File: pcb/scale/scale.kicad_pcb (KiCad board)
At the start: 2 copper layers, 103.8 x 47.9 mm, 86 parts, among them J1 USB_C_Receptacle_USB2.0, J2 Conn_01x07, J3 Conn_01x04, SW1 SW_Push, SW10 SW_Push, SW11 SW_Push, SW12 SW_Push, SW13 SW_Push, SW14 SW_Push, SW15 SW_Push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

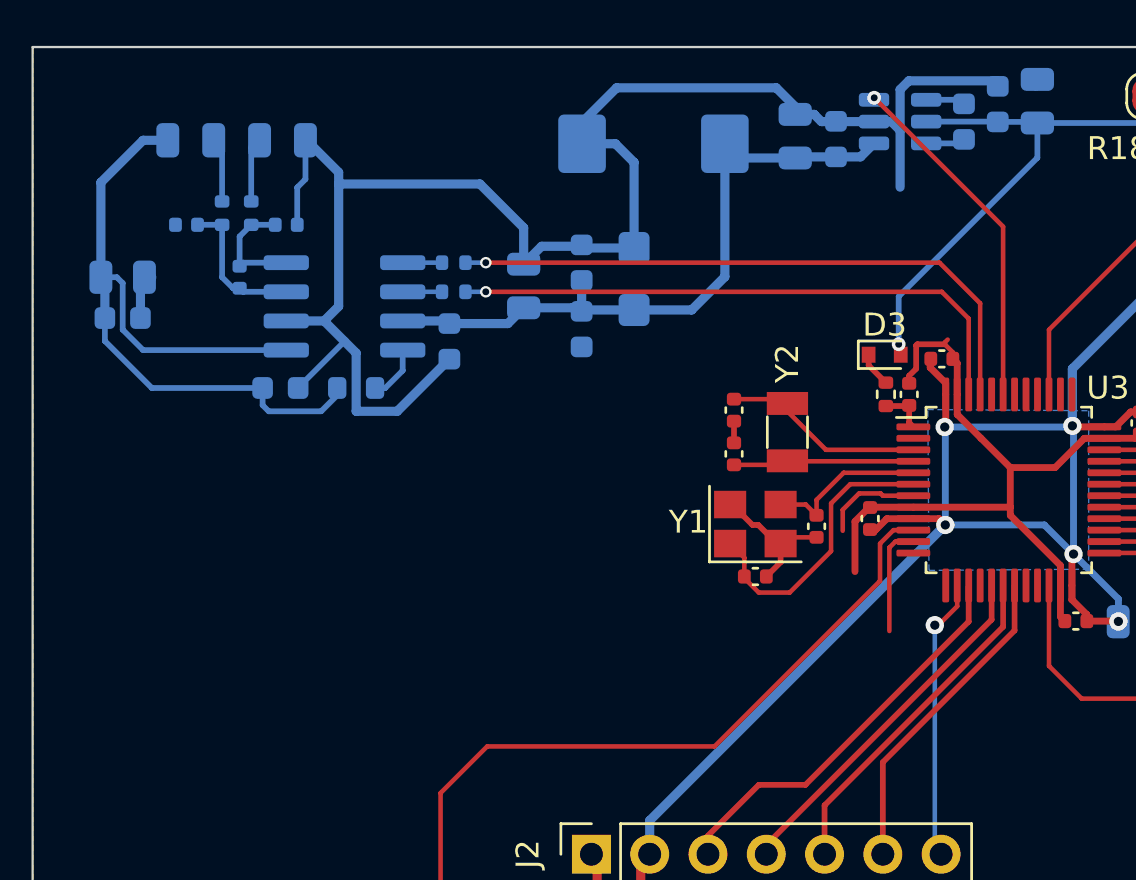
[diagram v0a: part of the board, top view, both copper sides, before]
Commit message: 移除0402元件位号，添加NRST和BOOT0电路
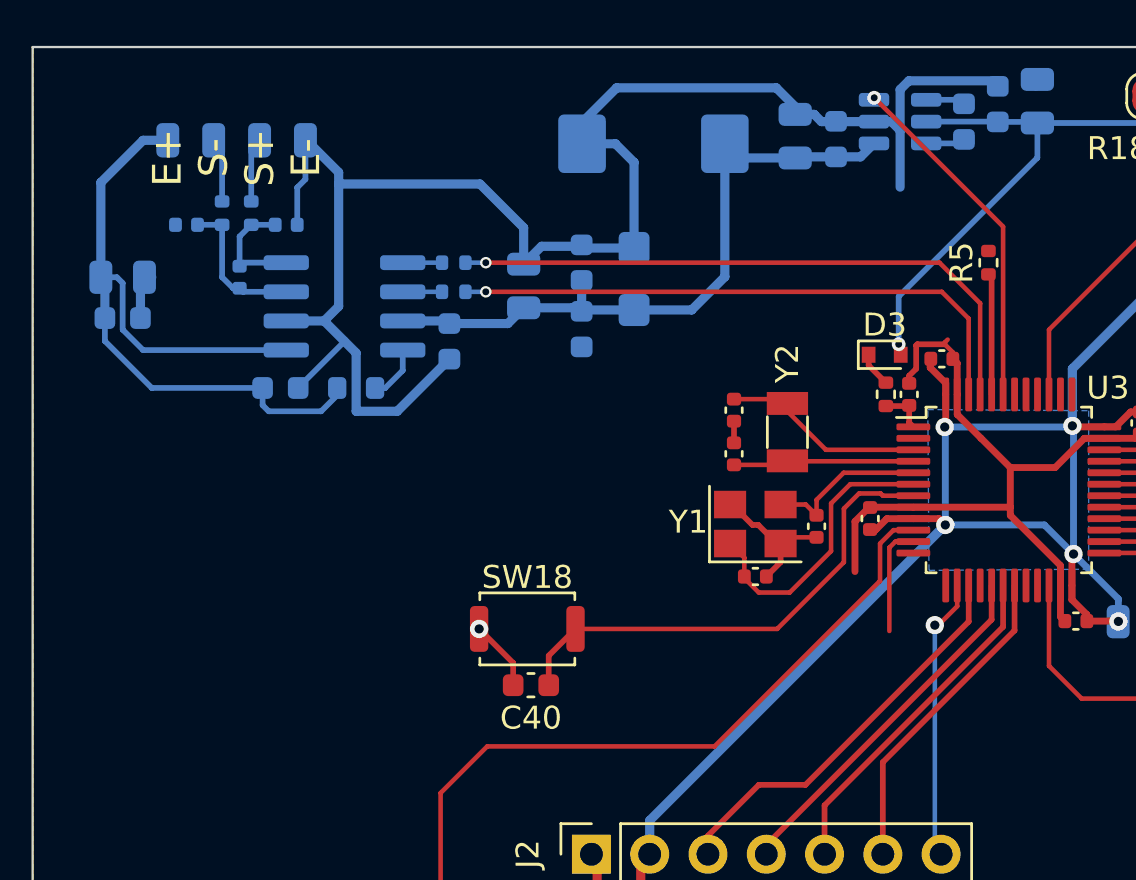
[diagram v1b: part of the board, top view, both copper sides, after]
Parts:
- added C40: 100n, Capacitor_SMD:C_0603_1608Metric, F.Cu at (90.8, 78.6)
- added R5: 47k, Resistor_SMD:R_0402_1005Metric, F.Cu at (110.7, 60.2)
- added SW18: SW_Push, Button_Switch_SMD:SW_Push_SPST_NO_Alps_SKRK, F.Cu at (90.6, 76.2)
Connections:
- U3 pad 44: unconnected-(U3-Pad44) -> /BOOT0
- U3 pad 7: unconnected-(U3-Pad7) -> /NRST
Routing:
- net /NRST: track 0.00 -> 21.5 mm
- net /BOOT0: track 0.00 -> 5.29 mm
- net unconnected-(U3-Pad7): track 4.33 -> 0.00 mm
- net GND: track 187.3 -> 190.4 mm, vias 2 -> 3
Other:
- board text added: "E+ S- S+ E-"

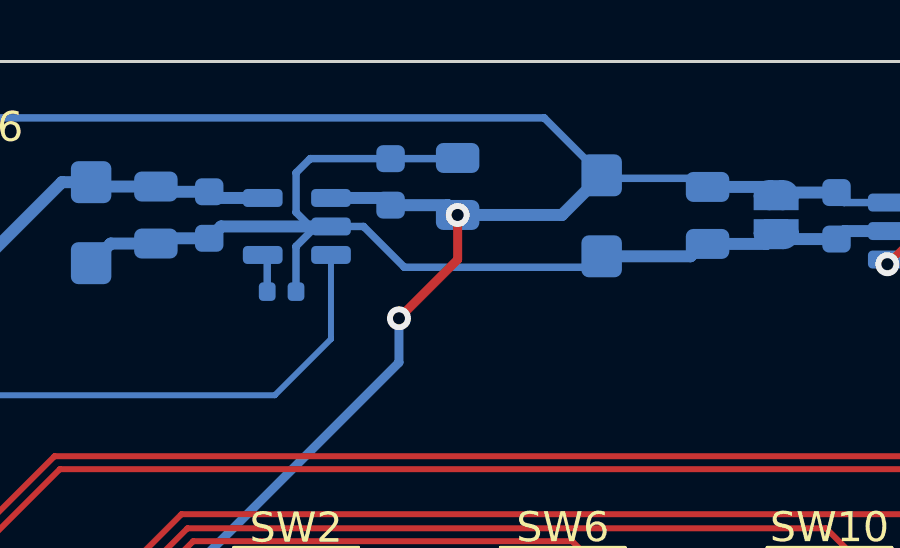
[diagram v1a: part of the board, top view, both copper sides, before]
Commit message: 数字LDO输入滤波电容旋转
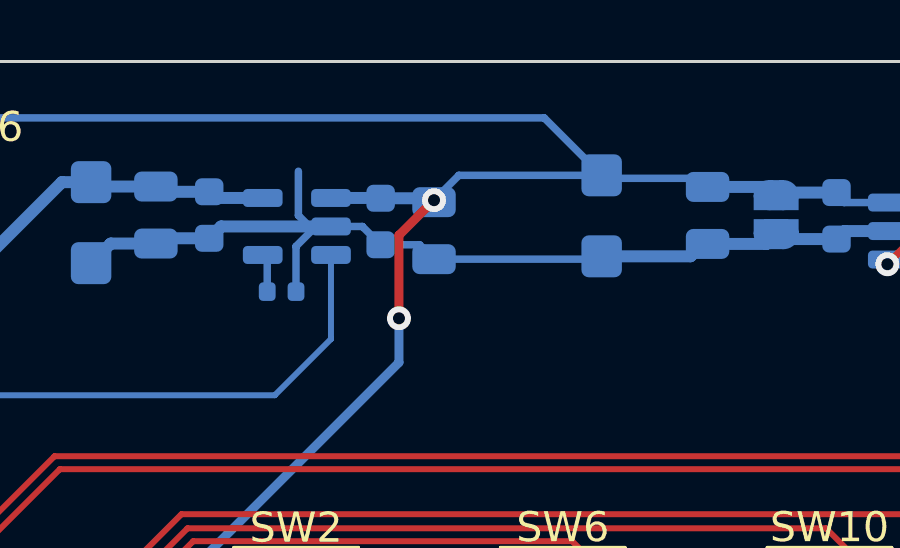
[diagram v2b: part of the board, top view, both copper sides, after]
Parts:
- moved C5 1.67 mm to (136.8, 56.4), turned to -90 degrees
- moved C7 1.36 mm to (135.0, 56.1), turned to -90 degrees
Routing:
- net GND: track 190.4 -> 185.8 mm

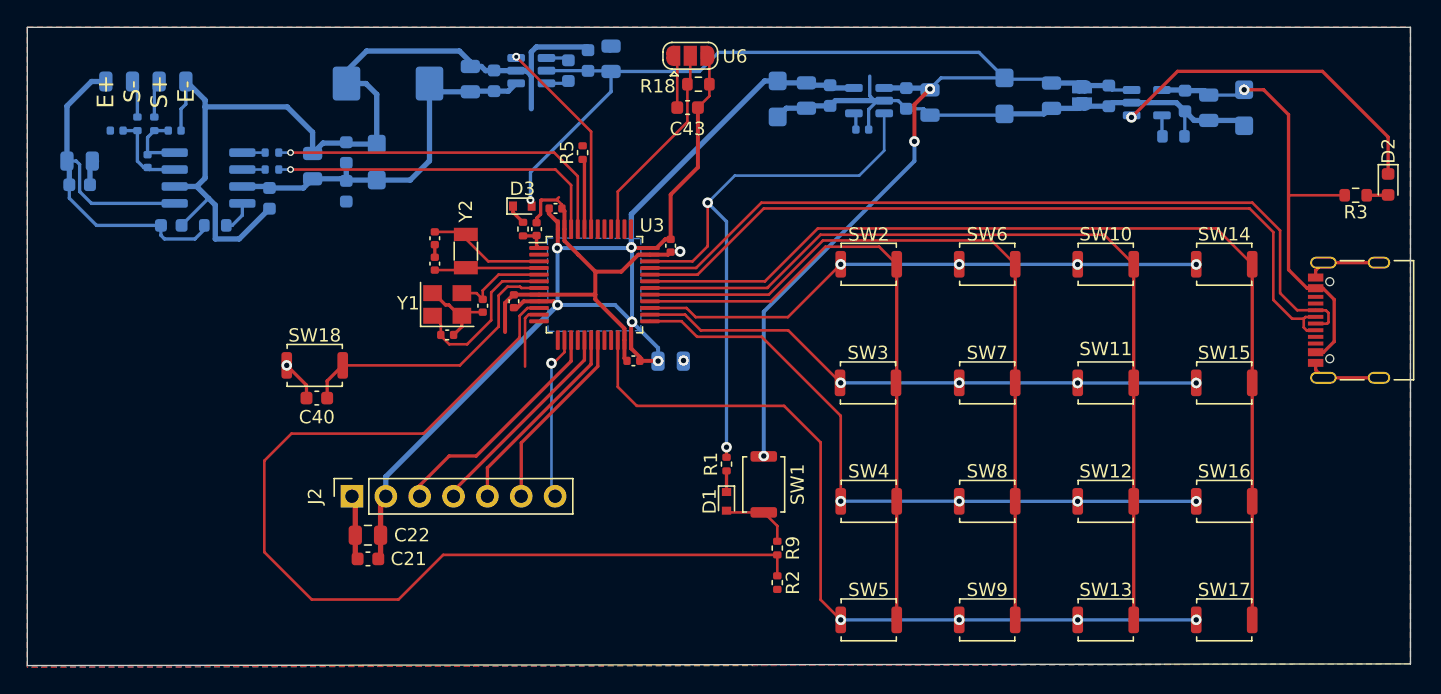
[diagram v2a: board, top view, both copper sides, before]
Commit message: 移动5V电荷泵电容，微调布线，修复一些DRC错误
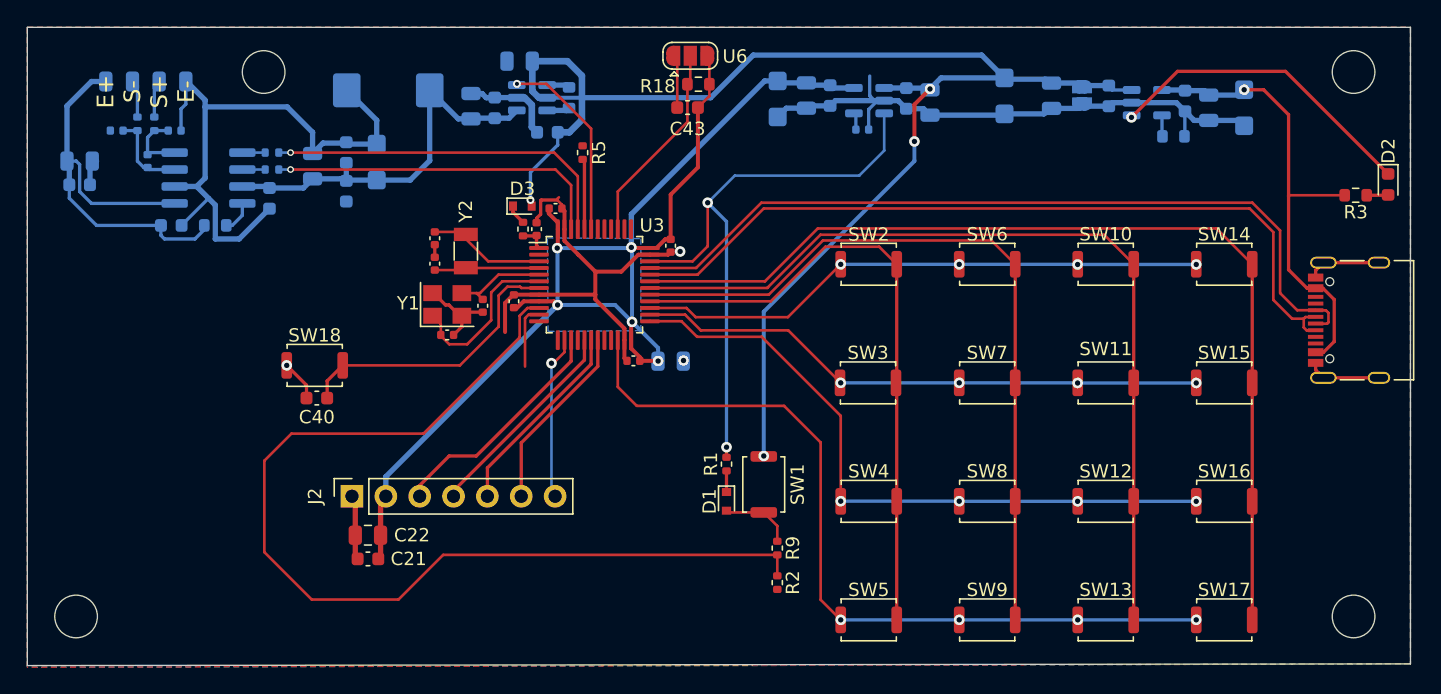
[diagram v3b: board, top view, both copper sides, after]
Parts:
- moved C27 6.86 mm to (106.0, 53.3), turned to 180 degrees
- moved C29 6.19 mm to (108.1, 58.7), turned to 180 degrees
- moved C33 2.03 mm to (102.4, 56.7)
- moved C23 2.03 mm to (104.2, 56.8)
- moved U4 2.03 mm to (106.9, 56.1)
- moved C31 2.03 mm to (109.7, 56.1)
- moved C34 0.51 mm to (96.2, 55.5)
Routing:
- net GND: track 185.8 -> 165.3 mm
- net +BATT: track 99.9 -> 107.5 mm
- net Net-(D2-Pad1): track 25.5 -> 23.9 mm
- net /APWR_EN: track 15.3 -> 14.5 mm
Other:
- outline, holes or cut-outs redrawn

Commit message: 添加一些GND过孔
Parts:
- moved C35 15.0 mm to (113.1, 64.7), turned to 180 degrees
- moved C20 10.4 mm to (107.9, 71.6), turned to 180 degrees
- moved C34 4.36 mm to (98.9, 59.0), turned to 90 degrees
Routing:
- net +3V3: track 103.3 -> 98.1 mm, vias 5 -> 4
- net unconnected-(U3-Pad11): track 4.79 -> 0.00 mm
- net +5V: track 29.0 -> 25.0 mm
- net GND: track 165.3 -> 166.4 mm, vias 3 -> 17

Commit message: 微调布线
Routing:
- net VBUS: track 35.6 -> 34.6 mm
- net GND: track 166.4 -> 165.9 mm
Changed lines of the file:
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@@
   (segment (start 73.787 61.008) (end 73.962 60.833) (width 0.4) (layer "B.Cu") (net 2))
   (segment (start 73.787 62.611) (end 73.787 61.008) (width 0.4) (layer "B.Cu") (net 2))
-  (segment (start 165.9335 76.7095) (end 166.315 77.091) (width 0.25) (layer "B.Cu") (net 2))
   (segment (start 93.151 59.5592) (end 93.0148 59.423) (width 0.4) (layer "B.Cu") (net 2))
   (segment (start 133.3699 56.2988) (end 129.7054 56.2988) (width 0.4) (layer "B.Cu") (net 2))
@@
   (segment (start 106.2736 66.4464) (end 107.2616 66.4464) (width 0.25) (layer "F.Cu") (net 11))
   (segment (start 107.2616 66.4464) (end 107.2896 66.4184) (width 0.25) (layer "F.Cu") (net 11))
+  (segment (start 115.7955 69.354) (end 119.368 69.354) (width 0.2) (layer "F.Cu") (net 12))
   (segment (start 164.9644 72.5334) (end 165.735 72.5334) (width 0.2) (layer "F.Cu") (net 12))
   (segment (start 165.735 73.5334) (end 165.058 73.5334) (width 0.2) (layer "F.Cu") (net 12))
   (segment (start 164.8414 73.3168) (end 164.8414 72.6564) (width 0.2) (layer "F.Cu") (net 12))
   (segment (start 165.058 73.5334) (end 164.8414 73.3168) (width 0.2) (layer "F.Cu") (net 12))
-  (segment (start 162.56 71.247) (end 163.9694 72.6564) (width 0.2) (layer "F.Cu") (net 12))
+  (segment (start 162.4 65.789) (end 162.4 70.819) (width 0.2) (layer "F.Cu") (net 12))
+  (segment (start 160.999 64.388) (end 162.4 65.789) (width 0.2) (layer "F.Cu") (net 12))
+  (segment (start 164.8414 72.6564) (end 164.9644 72.5334) (width 0.2) (layer "F.Cu") (net 12))
+  (segment (start 164.8404 72.6554) (end 164.8414 72.6564) (width 0.2) (layer "F.Cu") (net 12))
   (segment (start 119.368 69.354) (end 124.333 64.389) (width 0.2) (layer "F.Cu") (net 12))
-  (segment (start 115.7955 69.354) (end 119.368 69.354) (width 0.2) (layer "F.Cu") (net 12))
-  (segment (start 163.9694 72.6564) (end 164.8414 72.6564) (width 0.2) (layer "F.Cu") (net 12))
-  (segment (start 162.56 66.167) (end 162.56 71.247) (width 0.2) (layer "F.Cu") (net 12))
-  (segment (start 160.782 64.389) (end 162.56 66.167) (width 0.2) (layer "F.Cu") (net 12))
-  (segment (start 124.333 64.389) (end 160.782 64.389) (width 0.2) (layer "F.Cu") (net 12))
-  (segment (start 164.8414 72.6564) (end 164.9644 72.5334) (width 0.2) (layer "F.Cu") (net 12))
-  (segment (start 164.35 72.021) (end 165.735 72.021) (width 0.2) (layer "F.Cu") (net 13))
+  (segment (start 162.4 70.819) (end 164.2364 72.6554) (width 0.2) (layer "F.Cu") (net 12))
+  (segment (start 164.2364 72.6554) (end 164.8404 72.6554) (width 0.2) (layer "F.Cu") (net 12))
+  (segment (start 124.333 64.389) (end 160.998 64.389) (width 0.2) (layer "F.Cu") (net 12))
+  (segment (start 160.998 64.389) (end 160.999 64.388) (width 0.2) (layer "F.Cu") (net 12))
+  (segment (start 161.1572 63.9562) (end 162.81 65.609) (width 0.2) (layer "F.Cu") (net 13))
+  (segment (start 166.598 73.0334) (end 165.735 73.0334) (width 0.2) (layer "F.Cu") (net 13))
+  (segment (start 165.734 72.02) (end 165.735 72.021) (width 0.2) (layer "F.Cu") (net 13))
+  (segment (start 166.6956 72.2246) (end 166.6956 72.9358) (width 0.2) (layer "F.Cu") (net 13))
+  (segment (start 119.2584 68.854) (end 124.1552 63.9572) (width 0.2) (layer "F.Cu") (net 13))
+  (segment (start 166.492 72.021) (end 166.6956 72.2246) (width 0.2) (layer "F.Cu") (net 13))
+  (segment (start 162.81 65.609) (end 162.81 70.32) (width 0.2) (layer "F.Cu") (net 13))
+  (segment (start 124.1552 63.9572) (end 161.1562 63.9572) (width 0.2) (layer "F.Cu") (net 13))
+  (segment (start 162.81 70.32) (end 164.51 72.02) (width 0.2) (layer "F.Cu") (net 13))
+  (segment (start 164.51 72.02) (end 165.734 72.02) (width 0.2) (layer "F.Cu") (net 13))
+  (segment (start 161.1562 63.9572) (end 161.1572 63.9562) (width 0.2) (layer "F.Cu") (net 13))
   (segment (start 115.7955 68.854) (end 119.2584 68.854) (width 0.2) (layer "F.Cu") (net 13))
-  (segment (start 166.598 73.0334) (end 165.735 73.0334) (width 0.2) (layer "F.Cu") (net 13))
-  (segment (start 166.6956 72.2246) (end 166.6956 72.9358) (width 0.2) (layer "F.Cu") (net 13))
-  (segment (start 160.9852 63.9572) (end 163.068 66.04) (width 0.2) (layer "F.Cu") (net 13))
-  (segment (start 166.492 72.021) (end 166.6956 72.2246) (width 0.2) (layer "F.Cu") (net 13))
-  (segment (start 163.068 70.739) (end 164.35 72.021) (width 0.2) (layer "F.Cu") (net 13))
-  (segment (start 119.2584 68.854) (end 124.1552 63.9572) (width 0.2) (layer "F.Cu") (net 13))
-  (segment (start 163.068 66.04) (end 163.068 70.739) (width 0.2) (layer "F.Cu") (net 13))
-  (segment (start 124.1552 63.9572) (end 160.9852 63.9572) (width 0.2) (layer "F.Cu") (net 13))
   (segment (start 166.6956 72.9358) (end 166.598 73.0334) (width 0.2) (layer "F.Cu") (net 13))
   (segment (start 165.735 72.021) (end 166.492 72.021) (width 0.2) (layer "F.Cu") (net 13))
@@
   (segment (start 130.107 95.25) (end 138.997 95.25) (width 0.25) (layer "B.Cu") (net 43))
   (segment (start 138.997 95.25) (end 147.887 95.25) (width 0.25) (layer "B.Cu") (net 43))
-  (segment (start 161.8326 55.4828) (end 160.37115 55.4828) (width 0.25) (layer "F.Cu") (net 44))
-  (segment (start 163.703 63.4492) (end 163.703 57.3532) (width 0.25) (layer "F.Cu") (net 44))
-  (segment (start 163.703 57.3532) (end 161.8326 55.4828) (width 0.25) (layer "F.Cu") (net 44))
-  (segment (start 165.735 70.371) (end 165.0876 70.371) (width 0.25) (layer "F.Cu") (net 44))
-  (segment (start 166.3276 75.171) (end 167.1274 74.3712) (width 0.25) (layer "F.Cu") (net 44))
-  (segment (start 167.1274 71.2216) (end 167.1274 74.3712) (width 0.25) (layer "F.Cu") (net 44))
-  (segment (start 167.9133 63.3984) (end 163.7538 63.3984) (width 0.2) (layer "F.Cu") (net 44))
-  (segment (start 166.2768 70.371) (end 167.1274 71.2216) (width 0.25) (layer "F.Cu") (net 44))
-  (segment (start 163.703 68.9864) (end 163.703 63.4492) (width 0.25) (layer "F.Cu") (net 44))
-  (segment (start 163.7538 63.3984) (end 163.703 63.4492) (width 0.2) (layer "F.Cu") (net 44))
-  (segment (start 165.735 75.171) (end 166.3276 75.171) (width 0.25) (layer "F.Cu") (net 44))
-  (segment (start 165.735 70.371) (end 166.2768 70.371) (width 0.25) (layer "F.Cu") (net 44))
-  (segment (start 165.0876 70.371) (end 163.703 68.9864) (width 0.25) (layer "F.Cu") (net 44))
+  (segment (start 167.23 71.31) (end 167.23 74.27) (width 0.4) (layer "F.Cu") (net 44))
+  (segment (start 167.9133 63.3984) (end 167.9117 63.4) (width 0.2) (layer "F.Cu") (net 44))
+  (segment (start 166.329 75.171) (end 166.84 74.66) (width 0.25) (layer "F.Cu") (net 44))
+  (segment (start 167.23 74.27) (end 166.84 74.66) (width 0.4) (layer "F.Cu") (net 44))
+  (segment (start 163.95 69.76) (end 163.95 63.4) (width 0.4) (layer "F.Cu") (net 44))
+  (segment (start 166.84 70.92) (end 167.23 71.31) (width 0.4) (layer "F.Cu") (net 44))
+  (segment (start 165.735 70.371) (end 166.291 70.371) (width 0.25) (layer "F.Cu") (net 44))
+  (segment (start 165.4545 70.3505) (end 164.5405 70.3505) (width 0.4) (layer "F.Cu") (net 44))
+  (segment (start 163.95 59.06165) (end 160.37115 55.4828) (width 0.4) (layer "F.Cu") (net 44))
+  (segment (start 163.95 63.4) (end 163.95 59.06165) (width 0.4) (layer "F.Cu") (net 44))
+  (segment (start 165.735 75.171) (end 166.329 75.171) (width 0.25) (layer "F.Cu") (net 44))
+  (segment (start 164.5405 70.3505) (end 163.95 69.76) (width 0.4) (layer "F.Cu") (net 44))
+  (segment (start 167.9117 63.4) (end 163.95 63.4) (width 0.2) (layer "F.Cu") (net 44))
+  (segment (start 166.291 70.371) (end 166.84 70.92) (width 0.25) (layer "F.Cu") (net 44))
   (via (at 160.37115 55.4828) (size 0.8) (drill 0.4) (layers "F.Cu" "B.Cu") (net 44))
   (segment (start 155.9359 55.5498) (end 157.3809 55.5498) (width 0.4) (layer "B.Cu") (net 44))
